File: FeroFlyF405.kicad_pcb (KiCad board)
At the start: 2 copper layers, 153 parts, among them J301 Conn_01x04_Pin, J601 SM04B-GHS-TB(LF)(SN), J801 SM04B-GHS-TB(LF)(SN), J802 SM06B-GHS-TB(LF)(SN), J803 SM04B-GHS-TB(LF)(SN), J804 SM04B-GHS-TB(LF)(SN), J805 SM06B-GHS-TB(LF)(SN), J901 Conn_01x03_Pin, J902 Conn_01x03_Pin, J903 Conn_01x03_Pin, J904 Conn_01x03_Pin, J905 Conn_01x03_Pin, J906 Conn_01x03_Pin, J907 Conn_01x03_Pin, J908 Conn_01x03_Pin, J909 Conn_01x03_Pin, J910 Conn_01x03_Pin, J911 Conn_01x03_Pin, J912 Conn_01x03_Pin, J913 12402012E212A, J914 SM04B-GHS-TB(LF)(SN), SW301 SW_Push, SW302 SW_Push, U201 AP62200WU-7, U202 TLV75733PDRV, U301 STM32F405RGTx, U501 LSM6DSL, U502 BMP390, U601 SN65HVD230DR, U901 USBLC6-2P6, Y301 24MHz

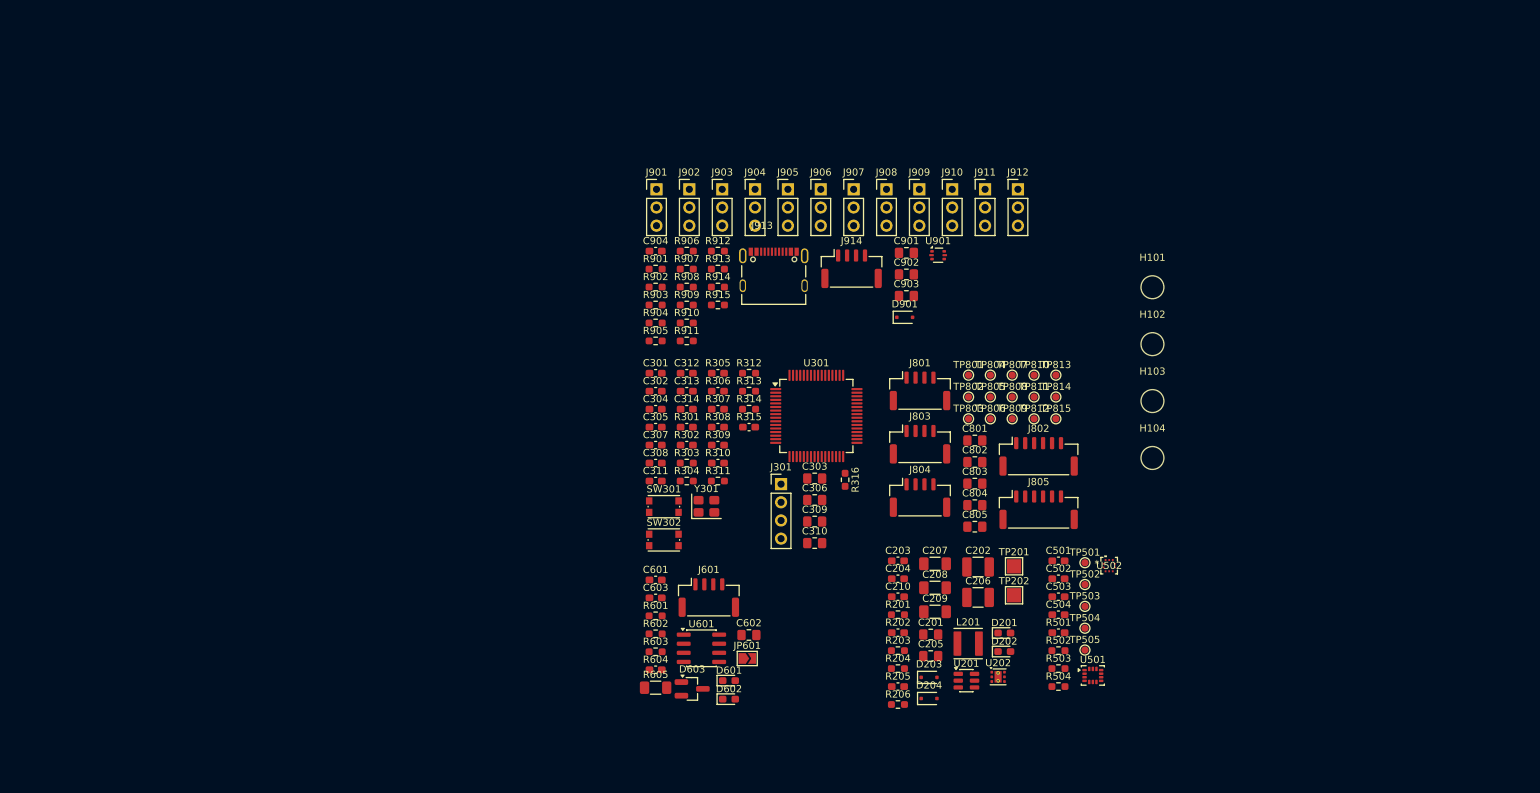
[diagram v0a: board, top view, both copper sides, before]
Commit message: feat: add intial PCB design & modify pin header lib
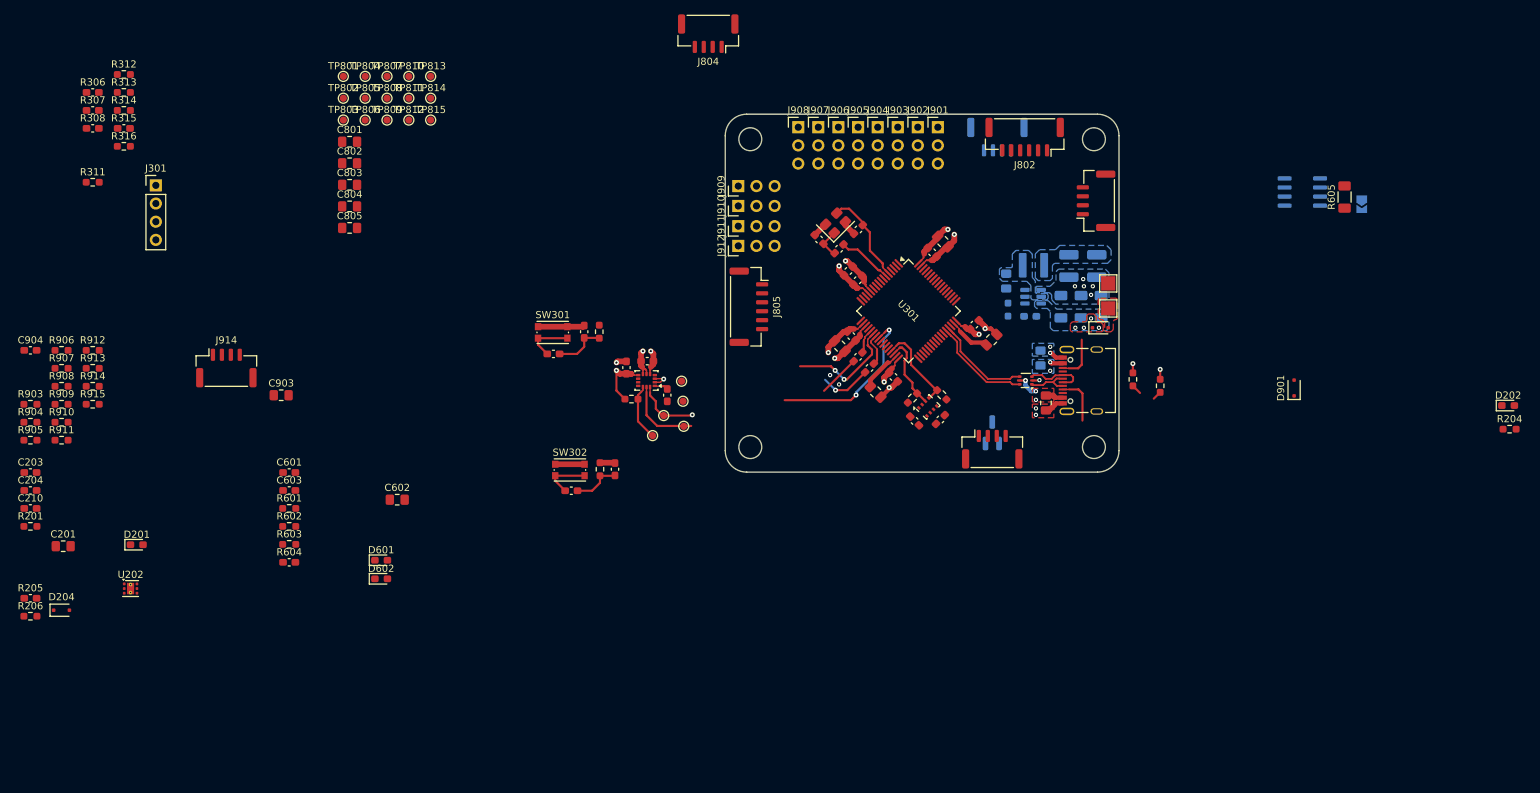
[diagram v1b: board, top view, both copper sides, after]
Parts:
- C202, C205, C206, C207, C208, C209, C901, D603, J803, JP601, L201, R202, R203, U201, U601: moved to B.Cu
- J901, J902, J903, J904, J905, J906, J907, J908, J909, J910, J911, J912: footprint Connector_PinHeader_2.54mm:PinHeader_1x03_P2.54mm_Vertical -> pin_header_01x03:PinHeader_1x03_P2.54mm_Vertical
- U502: value BMP390 -> DPS368; footprint BMP390:10LGA_2X2X0p75_BOS -> Package_LGA:Bosch_LGA-8_2x2.5mm_P0.65mm_ClockwisePinNumbering
- moved C201 121.8 mm to (35.5, 114.3)
- moved C203 121.8 mm to (30.9, 104.0)
- moved C204 121.8 mm to (30.9, 106.6)
- moved C210 121.8 mm to (30.9, 109.1)
- moved D204 121.8 mm to (35.3, 123.3)
- moved R201 121.8 mm to (30.9, 111.6)
- moved R205 121.8 mm to (30.9, 121.6)
- moved R206 121.8 mm to (30.9, 124.1)
- moved U202 121.8 mm to (44.9, 120.3)
- moved D201 121.8 mm to (45.8, 114.1)
- moved R605 118.1 mm to (214.5, 65.6), turned to 90 degrees
- moved R316 111.0 mm to (44.0, 58.5), turned to 0 degrees
- moved JP601 106.7 mm to (216.9, 66.6), turned to -90 degrees
- moved U601 105.4 mm to (208.6, 64.9)
- moved C801 96.8 mm to (75.5, 57.9)
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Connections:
- net /MCU/D_PA5 renamed /MCU/SPI1_SCKR
- net /MCU/D_PA7 renamed /MCU/SPI1_MOSIR
- net /MCU/D_SPI1_CS renamed /MCU/SPI1_CS
- net /MCU/D_SPI1_MISO renamed /MCU/SPI1_MISO
- net /MCU/D_SPI1_MOSI renamed /MCU/SPI1_MOSI
- net /MCU/D_SPI1_SCK renamed /MCU/SPI1_SCK
- net /Peripherals/IMUs/D_SPI1_MISOR renamed /Peripherals/IMUs/SPI1_MISOR
- net Net-(JP601-B) renamed /Peripherals/CAN & LEDs/D_CANTR
- D603 pad 1: /Peripherals/CAN & LEDs/CAN- -> /Peripherals/CAN & LEDs/CAN+
- D603 pad 2: /Peripherals/CAN & LEDs/CAN+ -> /Peripherals/CAN & LEDs/CAN-
- U301 pad 44: /IO/USB_D+ -> /IO/USB_D-
- U301 pad 45: /IO/USB_D- -> /IO/USB_D+
- U502 pad 1: +3V3 -> GND
- U502 pad 2: /MCU/D_I2C2_SCL -> +3V3
- U502 pad 3: GND -> /MCU/D_I2C2_SDA
- U502 pad 4: /MCU/D_I2C2_SDA -> /MCU/D_I2C2_SCL
- U502 pad 5: GND -> unconnected-(U502-SDO-Pad5)
- U502 pad 7: unconnected-(U502-INT-Pad7) -> GND
- U502 pad 8: GND -> +3V3
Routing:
- net GND: track 0.00 -> 55.5 mm, vias 0 -> 22
- net +3V3: track 0.00 -> 40.6 mm, vias 0 -> 7
- net /MCU/SPI1_CS: track 0.00 -> 31.2 mm, vias 0 -> 2
- net /MCU/SPI1_SCK: track 0.00 -> 16.7 mm
- net /MCU/SPI1_MOSI: track 0.00 -> 16.1 mm, vias 0 -> 2
- net /MCU/SPI1_MISO: track 0.00 -> 15.8 mm, vias 0 -> 2
- net /IO/USB_D-: track 0.00 -> 14.3 mm
- net /IO/USB_D+: track 0.00 -> 13.9 mm
- net /MCU/D_OSC_IN: track 0.00 -> 13.3 mm
- net /MCU/D_I2C2_SCL: track 0.00 -> 12.5 mm
- net /MCU/D_I2C2_SDA: track 0.00 -> 10.6 mm
- net /IO/IO2/D_CC1A: track 0.00 -> 8.17 mm
- net /IO/IO2/USB_DP: track 0.00 -> 7.96 mm
- net /MCU/D_OSC_OUT: track 0.00 -> 7.80 mm
- net /IO/IO2/P_VBUS: track 0.00 -> 7.66 mm, vias 0 -> 5
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- added copper zone on B.Cu, net +5V
- added copper zone on B.Cu, net /IO/IO2/P_VBUS
- added copper zone on F.Cu, net /IO/IO2/P_VBUS
- added copper zone on B.Cu, net /Power/P_SW
- added copper zone on F.Cu, net /Power/P_VIN
- added copper zone on B.Cu, net GND
- added copper zone on F.Cu, net GND
- added copper zone on In1.Cu, net GND
- added copper zone on In2.Cu, net GND
- added copper zone on B.Cu, net VBAT
- added copper zone on F.Cu, net VBAT
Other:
- board outline added: 55 x 50 mm
- copper layers 2 -> 4
- rule pad_to_mask_clearance: 0 -> 0.06

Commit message: chore: initial PCB layout
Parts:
- C803, C804, C805, C902, C903, D901, J804, J805, J914, R312, R314, R904, R905, R906, R907, R908, R909, R910, R911, R912, R913, R914, R915: moved to B.Cu
- D603: footprint Package_TO_SOT_SMD:SOT-23_Handsoldering -> Package_TO_SOT_SMD:SOT-23; moved to F.Cu
- JP601, U601: moved to F.Cu
- U202: footprint Package_SON:WSON-6-1EP_2x2mm_P0.65mm_EP1x1.6mm_ThermalVias -> Package_SON:WSON-6-1EP_2x2mm_P0.65mm_EP1x1.6mm
- moved R904 137.4 mm to (167.1, 78.5), turned to 180 degrees
- moved R905 137.4 mm to (167.1, 81.3), turned to 180 degrees
- moved R911 131.9 mm to (167.2, 98.0), turned to 180 degrees
- moved R907 131.8 mm to (167.1, 86.9), turned to 180 degrees
- moved R908 131.8 mm to (167.1, 89.7), turned to 180 degrees
- moved R906 131.8 mm to (167.1, 84.1), turned to 180 degrees
- moved R910 131.8 mm to (167.1, 95.3), turned to 180 degrees
- moved R909 131.8 mm to (167.1, 92.4), turned to 180 degrees
- moved R913 128.4 mm to (167.3, 103.8), turned to 180 degrees
- moved R915 128.4 mm to (167.2, 109.4), turned to 180 degrees
- moved R914 128.4 mm to (167.2, 106.7), turned to 180 degrees
- moved R912 128.3 mm to (167.2, 100.9), turned to 180 degrees
- moved R315 119.2 mm to (159.7, 84.7), turned to 90 degrees
- moved R306 117.8 mm to (156.0, 69.5), turned to 45 degrees
- moved R307 116.8 mm to (156.1, 62.7), turned to 90 degrees
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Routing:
- net +5V: track 0.00 -> 196.7 mm, vias 0 -> 8
- net +3V3: track 40.6 -> 176.3 mm, vias 7 -> 12
- net /IO/D_TIM5_CH1: track 0.00 -> 43.5 mm, vias 0 -> 1
- net /IO/D_TIM2_CH1: track 0.00 -> 36.4 mm, vias 0 -> 1
- net /IO/D_TIM12_CH1: track 0.00 -> 33.6 mm, vias 0 -> 3
- net GND: track 55.5 -> 86.6 mm, vias 22 -> 66
- net /IO/D_TIM12_CH2: track 0.00 -> 29.1 mm, vias 0 -> 3
- net /IO/D_TIM8_CH2: track 0.00 -> 26.5 mm, vias 0 -> 1
- net /Peripherals/CAN & LEDs/CAN+: track 0.00 -> 25.5 mm, vias 0 -> 2
- net /IO/D_I2C1_SCL: track 0.00 -> 24.9 mm, vias 0 -> 2
- net /IO/D_TIM8_CH1: track 0.00 -> 24.5 mm, vias 0 -> 1
- net /IO/D_TIM4_CH4: track 0.00 -> 23.6 mm, vias 0 -> 1
- net /MCU/D_CAN2RX: track 0.00 -> 21.4 mm
- net /IO/D_TIM4_CH3: track 0.00 -> 20.9 mm, vias 0 -> 1
- net /IO/D_TIM3_CH3: track 0.00 -> 20.1 mm, vias 0 -> 1
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- added copper zone on F.Cu, net +3V3
- removed copper zone on F.Cu, net /IO/IO2/P_VBUS
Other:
- board size 55 x 50 mm -> 50 x 65 mm

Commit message: feat: more routing & add design rule clearance exclusion for IMU
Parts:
- added REF**: OSHW-Logo2_9.8x8mm_SilkScreen, Symbol:OSHW-Logo2_9.8x8mm_SilkScreen, F.Cu at (142.0, 101.4)
- C805, J804: moved to F.Cu
- C904, D204, R316, R903: moved to B.Cu
- moved R903 112.8 mm to (140.2, 66.4), turned to 180 degrees
- moved C904 111.6 mm to (141.1, 69.1), turned to -90 degrees
- moved R205 108.0 mm to (134.7, 91.7), turned to 90 degrees
- moved C210 107.3 mm to (136.8, 91.7), turned to -90 degrees
- moved R206 106.7 mm to (132.6, 91.7), turned to -90 degrees
- moved R602 103.1 mm to (170.1, 116.2), turned to -90 degrees
- moved R601 99.1 mm to (165.9, 116.2), turned to -90 degrees
- moved D602 88.2 mm to (168.1, 116.2), turned to 90 degrees
- moved D601 84.0 mm to (163.9, 116.1), turned to 90 degrees
- moved R201 70.5 mm to (141.7, 115.7), turned to 90 degrees
- moved TP805 67.2 mm to (135.8, 85.6)
- moved TP806 63.3 mm to (133.7, 84.3)
- moved D201 58.9 mm to (144.0, 115.7), turned to 90 degrees
- moved TP504 53.9 mm to (155.7, 92.5)
- moved TP505 36.6 mm to (145.8, 91.6)
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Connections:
- C207 pad 1: VBAT -> /Power/P_VIN
- C208 pad 1: VBAT -> /Power/P_VIN
- C209 pad 1: VBAT -> /Power/P_VIN
- C210 pad 1: /MCU/D_ADC1_CH11 -> /MCU/D_ADC2_CH13
- C904 pad 1: /IO/D_ADC2_CH12 -> /IO/D_ADC1_CH10
- D203 pad 1: VBAT -> /Power/P_VIN
- D203 pad 2: /Power/P_VIN -> /Power/P_VBAT
- R205 pad 1: VBAT -> /Power/P_VBAT
- R205 pad 2: /MCU/D_ADC1_CH11 -> /MCU/D_ADC2_CH13
- R206 pad 1: /MCU/D_ADC1_CH11 -> /MCU/D_ADC2_CH13
- R903 pad 1: /IO/D_ADC2_CH12 -> /IO/D_ADC1_CH10
- R904 pad 2: /IO/D_TIM4_CH3 -> /IO/D_TIM1_CH2
- R905 pad 2: /IO/D_TIM4_CH4 -> /IO/D_TIM4_CH3
- R906 pad 2: /IO/D_TIM1_CH2 -> /IO/D_TIM4_CH4
- TP201 pad 1: /Power/P_VIN -> /Power/P_VBAT
- TP504 pad 1: /MCU/SPI1_CS -> GND
- U201 pad 3: VBAT -> /Power/P_VIN
- U301 pad 10: /IO/D_ADC2_CH12 -> /MCU/D_LED1
- U301 pad 11: unconnected-(U301-PC3-Pad11) -> /MCU/D_ADC2_CH13
- U301 pad 26: /MCU/D_LED0 -> unconnected-(U301-PB0-Pad26)
- U301 pad 27: /MCU/D_LED1 -> unconnected-(U301-PB1-Pad27)
- U301 pad 8: unconnected-(U301-PC0-Pad8) -> /IO/D_ADC1_CH10
- U301 pad 9: /MCU/D_ADC1_CH11 -> /MCU/D_LED0
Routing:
- net /IO/P_LDOIN: track 0.00 -> 77.8 mm, vias 0 -> 2
- net GND: track 86.6 -> 144.2 mm, vias 66 -> 96
- net /IO/D_PINIO1: track 0.00 -> 27.3 mm, vias 0 -> 2
- net /IO/D_PINIO0: track 0.00 -> 27.2 mm, vias 0 -> 2
- net /MCU/D_ADC2_CH13: track 0.00 -> 23.2 mm, vias 0 -> 2
- net /IO/D_USART2_RX: track 0.00 -> 20.3 mm, vias 0 -> 1
- net /IO/D_ADC1_CH10: track 0.00 -> 16.9 mm, vias 0 -> 1
- net +3V3: track 176.3 -> 192.6 mm
- net /MCU/D_BOOT0: track 6.63 -> 21.1 mm, vias 0 -> 2
- net /MCU/D_NRST: track 6.29 -> 17.3 mm, vias 0 -> 2
- net /IO/IO2/D_CUR: track 0.00 -> 10.2 mm, vias 0 -> 2
- net +5V: track 196.7 -> 204.0 mm, vias 8 -> 10
- net /IO/D_TIM1_CH2: track 17.3 -> 10.8 mm
- net /Power/P_VBAT: track 0.00 -> 6.21 mm
- net /MCU/D_PC12: track 10.3 -> 4.85 mm
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- added copper zone on F.Cu, net /IO/P_LDOIN
- added copper zone on F.Cu, net /Power/P_VBAT
- added copper zone on B.Cu, net /Power/P_VIN
- removed copper zone on B.Cu, net VBAT
- removed copper zone on F.Cu, net VBAT
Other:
- board text added: "3V3"
- board text added: "5V"
- board text added: "BAT+"
- board text added: "BAT-"
- board text added: "BOOT"
- board text added: "LED0"
- board text added: "LED1"
- board text added: "RST"
- board text added: "S1"
- board text added: "S2"

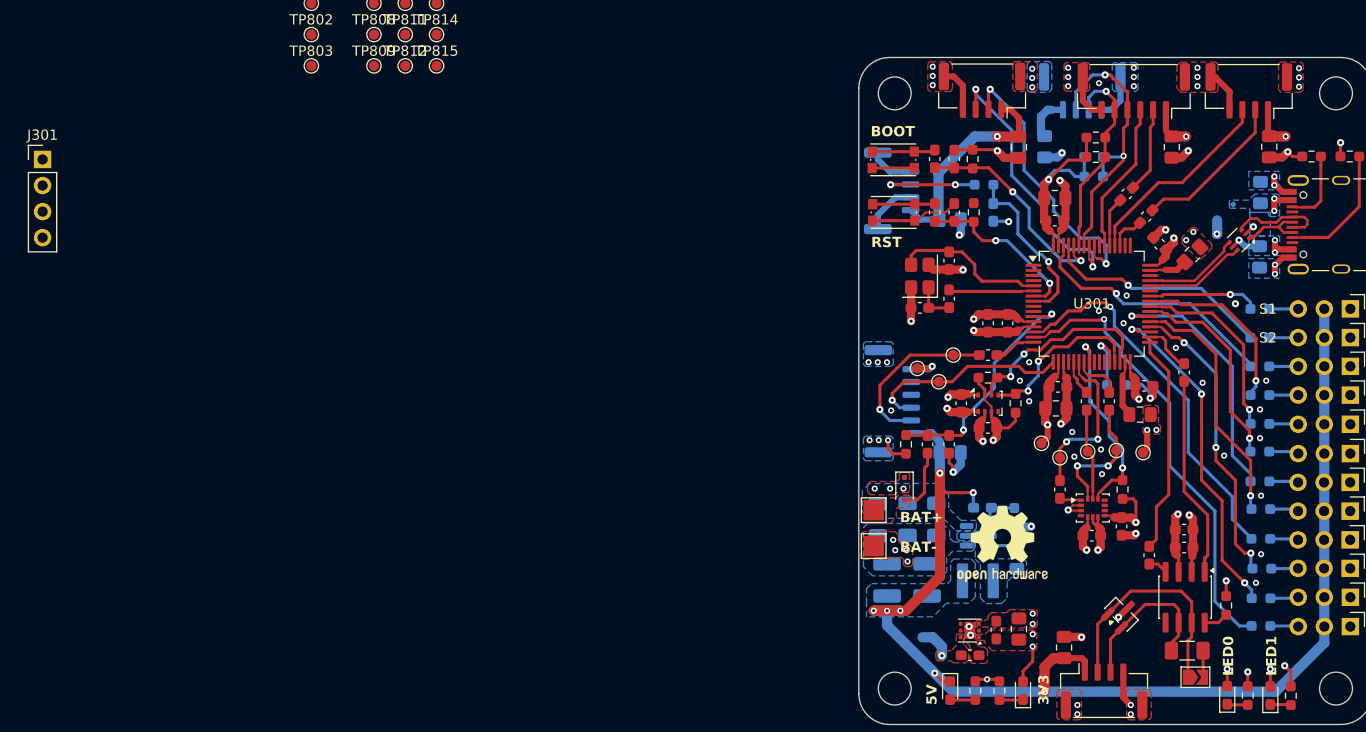
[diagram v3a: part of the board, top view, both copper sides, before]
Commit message: feat:  change SWD connector, route SWD signal & LEDs
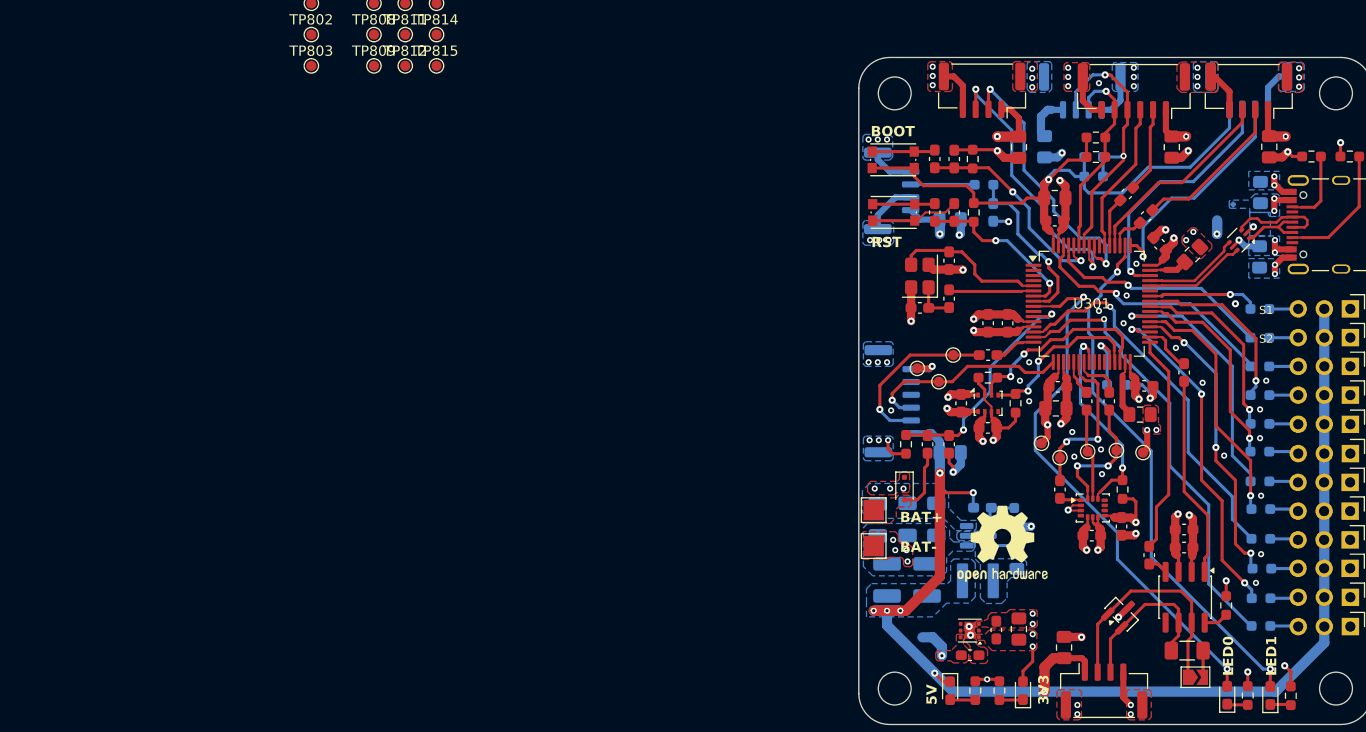
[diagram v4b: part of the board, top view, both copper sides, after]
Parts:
- removed J301: Conn_01x04_Pin, Connector_PinHeader_2.54mm:PinHeader_1x04_P2.54mm_Vertical
- added J302: SM04B-GHS-TB(LF)(SN), Connector_JST:JST_GH_SM04B-GHS-TB_1x04-1MP_P1.25mm_Horizontal, B.Cu at (166.0, 57.2)
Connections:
- U301 pad 10: /MCU/D_LED1 -> unconnected-(U301-PC2-Pad10)
- U301 pad 50: unconnected-(U301-PA15-Pad50) -> /MCU/D_LED1
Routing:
- net /MCU/D_LED0: track 1.67 -> 52.9 mm, vias 1 -> 2
- net /MCU/D_LED1: track 1.70 -> 52.2 mm, vias 1 -> 2
- net +3V3: track 192.6 -> 227.5 mm
- net /MCU/D_SWDIO: track 0.00 -> 24.4 mm, vias 0 -> 1
- net /MCU/D_SWCLK: track 0.00 -> 22.1 mm, vias 0 -> 1
- net GND: track 144.2 -> 148.7 mm, vias 96 -> 103
- net /IO/IO2/D_CUR: track 10.2 -> 6.25 mm, vias 2 -> 0
- net +5V: track 204.0 -> 206.7 mm, vias 10 -> 11
- net /IO/D_TIM5_CH1: track 44.1 -> 43.5 mm
- net /MCU/SPI1_CS: track 19.4 -> 20.0 mm
